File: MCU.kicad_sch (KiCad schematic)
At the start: 34 parts, among them J7 Microsemi_FlashPro-JTAG-10, SW3 SW_Push, SW4 SW_Push, U2 STM32F405RGTx, Y1 8mhz

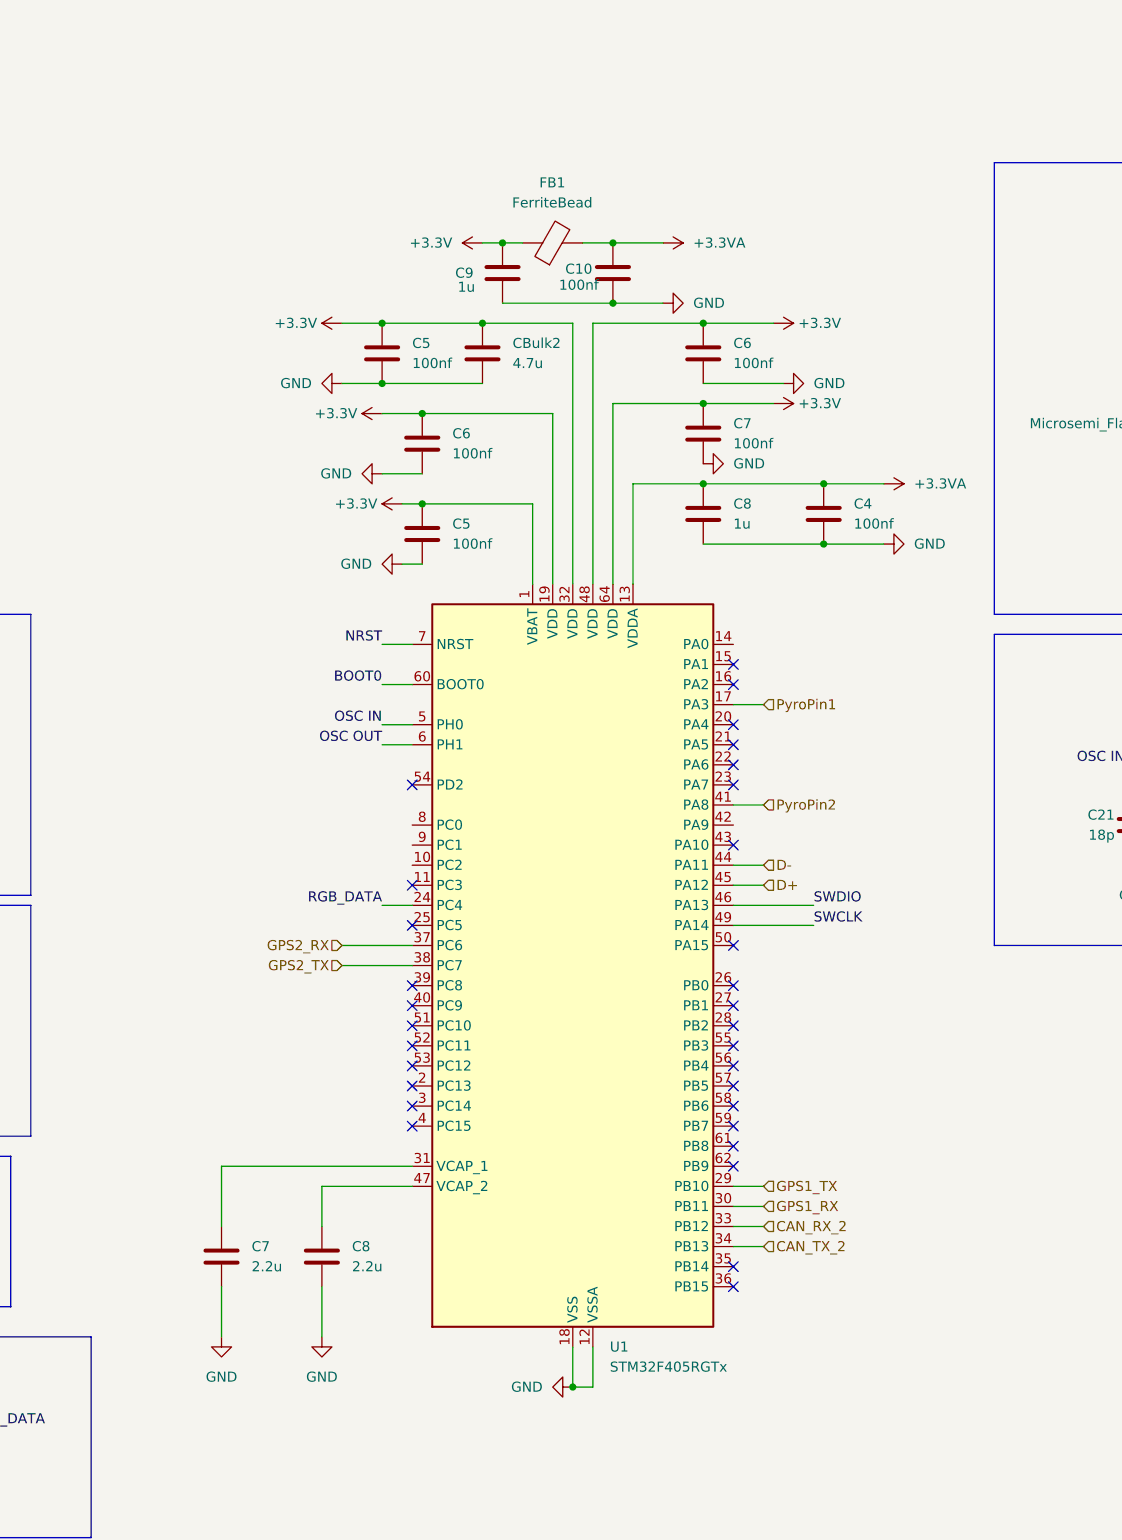
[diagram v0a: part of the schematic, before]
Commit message: began fixing schematic added barometer
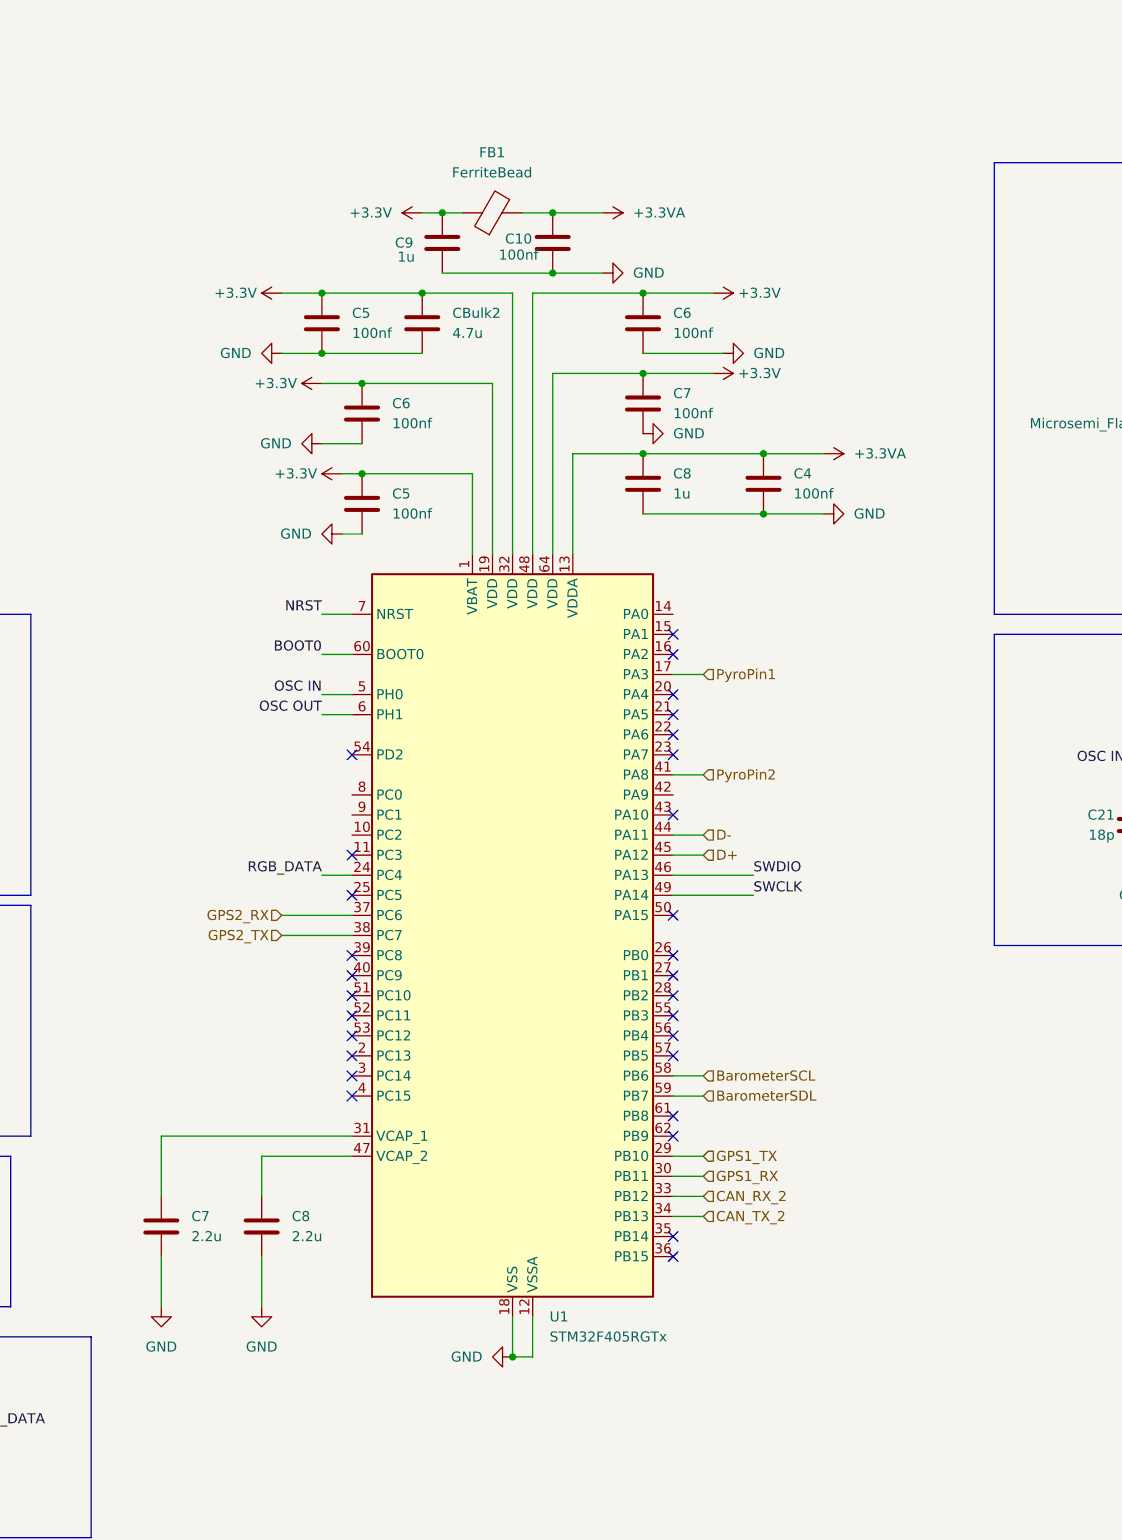
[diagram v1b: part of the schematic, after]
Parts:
- added C11: 1u, Capacitor_SMD:C_0805_2012Metric_Pad1.18x1.45mm_HandSolder, symbol Device:C
- added C12: 10u, Capacitor_SMD:C_0805_2012Metric_Pad1.18x1.45mm_HandSolder, symbol Device:C
- added C13, C14: 2.2u, Capacitor_SMD:C_0805_2012Metric_Pad1.18x1.45mm_HandSolder, symbol Device:C
- added C17, C18, C19, C3: 100nf, Capacitor_SMD:C_0805_2012Metric_Pad1.18x1.45mm_HandSolder, symbol Device:C
- added CBulk1: 4.7u, Capacitor_SMD:C_0805_2012Metric_Pad1.18x1.45mm_HandSolder, symbol Device:C
- added FB2: FerriteBead, Resistor_SMD:R_0805_2012Metric_Pad1.20x1.40mm_HandSolder, symbol Device:FerriteBead
- added U2: STM32F405RGTx, Package_QFP:LQFP-64_10x10mm_P0.5mm, symbol MCU_ST_STM32F4:STM32F405RGTx
- C10: renamed from C12; value 10u -> 100nf
- renumbered C3 to C16, C17 to C4, C18 to C5, C19 to C6, C13 to C7, C14 to C8, C11 to C9, CBulk1 to CBulk2, FB2 to FB1, U2 to U1
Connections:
- net +3.3V: now also C17.1, C18.1, C19.1, CBulk1.1, FB2.1, U2.1 (VBAT), U2.13 (VDDA), U2.19 (VDD), U2.32 (VDD), U2.48 (VDD), U2.64 (VDD); no longer C4.1, U1.13 (VDDA)
- net +3.3VA: now also C11.2, C12.2, FB2.2; no longer C9.2
- net BOOT0: now also U2.60 (BOOT0)
- net CAN_RX_2: now also U2.33 (PB12)
- net CAN_TX_2: now also U2.34 (PB13)
- net D+: now also U2.45 (PA12)
- net D-: now also U2.44 (PA11)
- net GND: now also C11.1, C12.1, C13.2, C14.2, C17.2, C18.2, C19.2, CBulk1.2, U2.12 (VSSA), U2.18 (VSS), U2.63 (VSS)
- net GPS1_RX: now also U2.30 (PB11)
- net GPS1_TX: now also U2.29 (PB10)
- net GPS2_RX: now also U2.37 (PC6)
- net GPS2_TX: now also U2.38 (PC7)
- net NRST: now also C3.1, U2.7 (NRST)
- net PA3: now also U2.17 (PA3); no longer U1.17 (PA3)
- net PA8: now also U2.41 (PA8); no longer U1.41 (PA8)
- net PA9: now also U2.42 (PA9); no longer U1.42 (PA9)
- net UART_DEBUG_RX: now also U2.54 (PD2); no longer U1.54 (PD2)
- net UART_DEBUG_TX: now also U2.53 (PC12); no longer U1.53 (PC12)
- net VBUS: now also U2.46 (PA13); no longer U1.46 (PA13)
- net at SW3.2: now also C3.2; no longer C16.2
- net BarometerSCL: now reaches U1.58 (PB6)
- net BarometerSDL: now reaches U1.59 (PB7)
- new net: C13.1, U2.31 (VCAP_1)
- new net: C14.1, U2.47 (VCAP_2)
- no-connect marks 36 -> 34
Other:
- moved on the sheet: C10, C4, C5, C6, C7, C8, C9, CBulk2, FB1, U1
